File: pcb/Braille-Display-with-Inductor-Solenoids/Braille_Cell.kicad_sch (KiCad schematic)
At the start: 12 parts, among them U2 AD116, U3 AD116

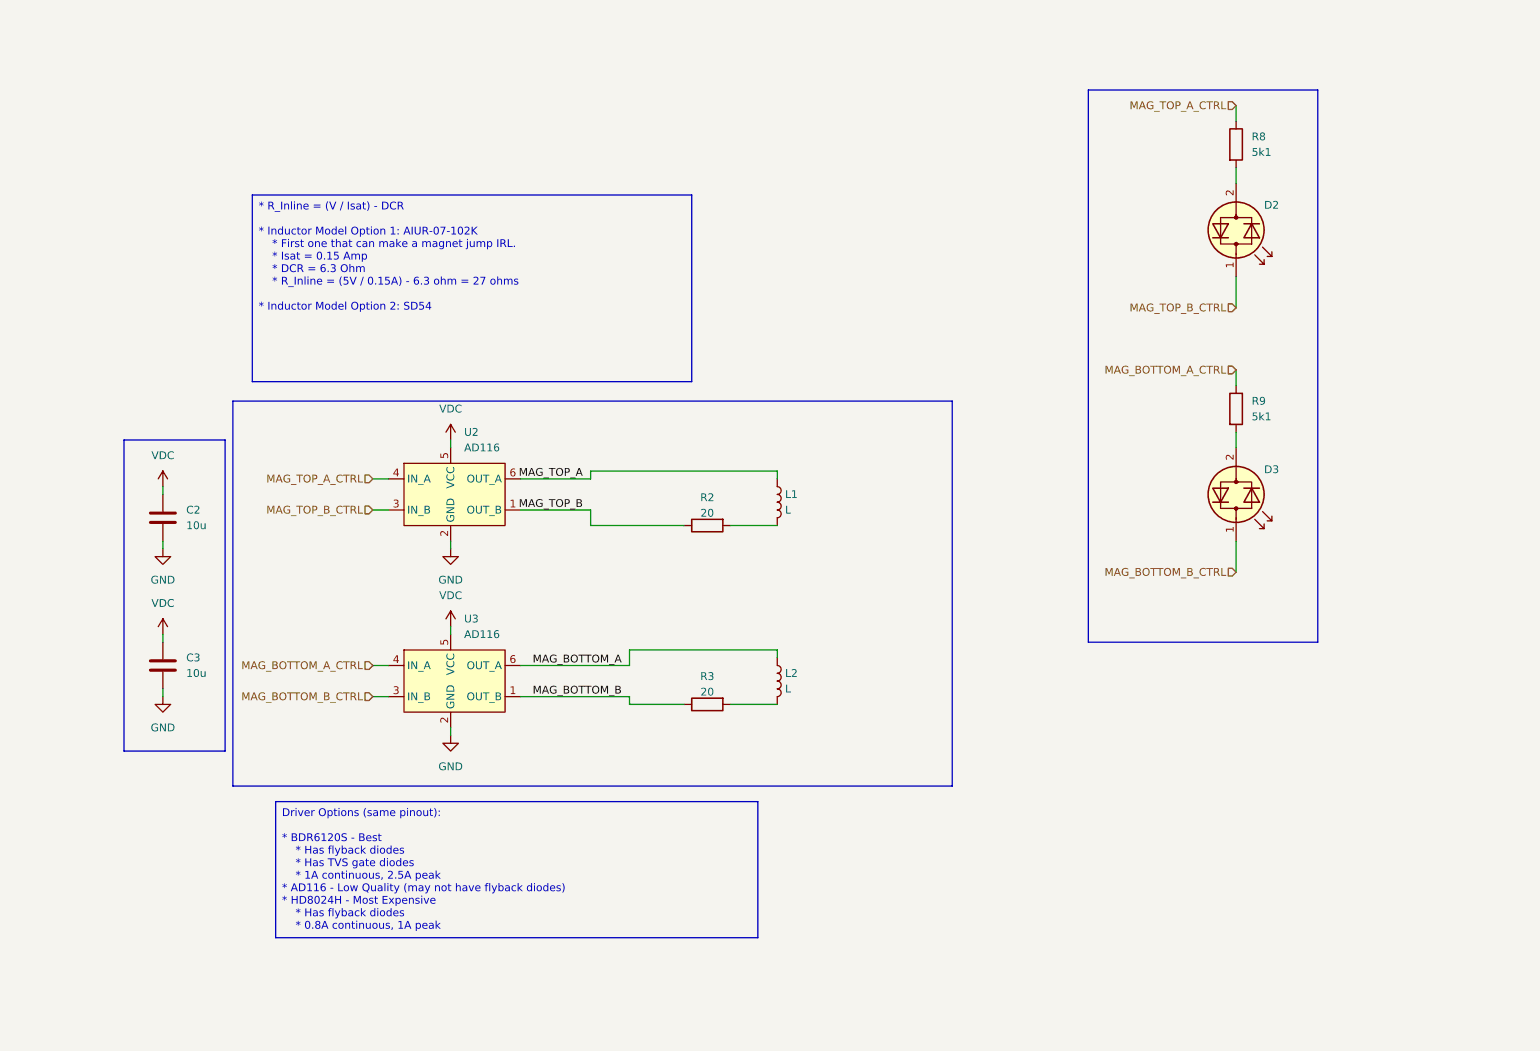
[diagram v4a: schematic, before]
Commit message: Bit of tiny routing, export production file
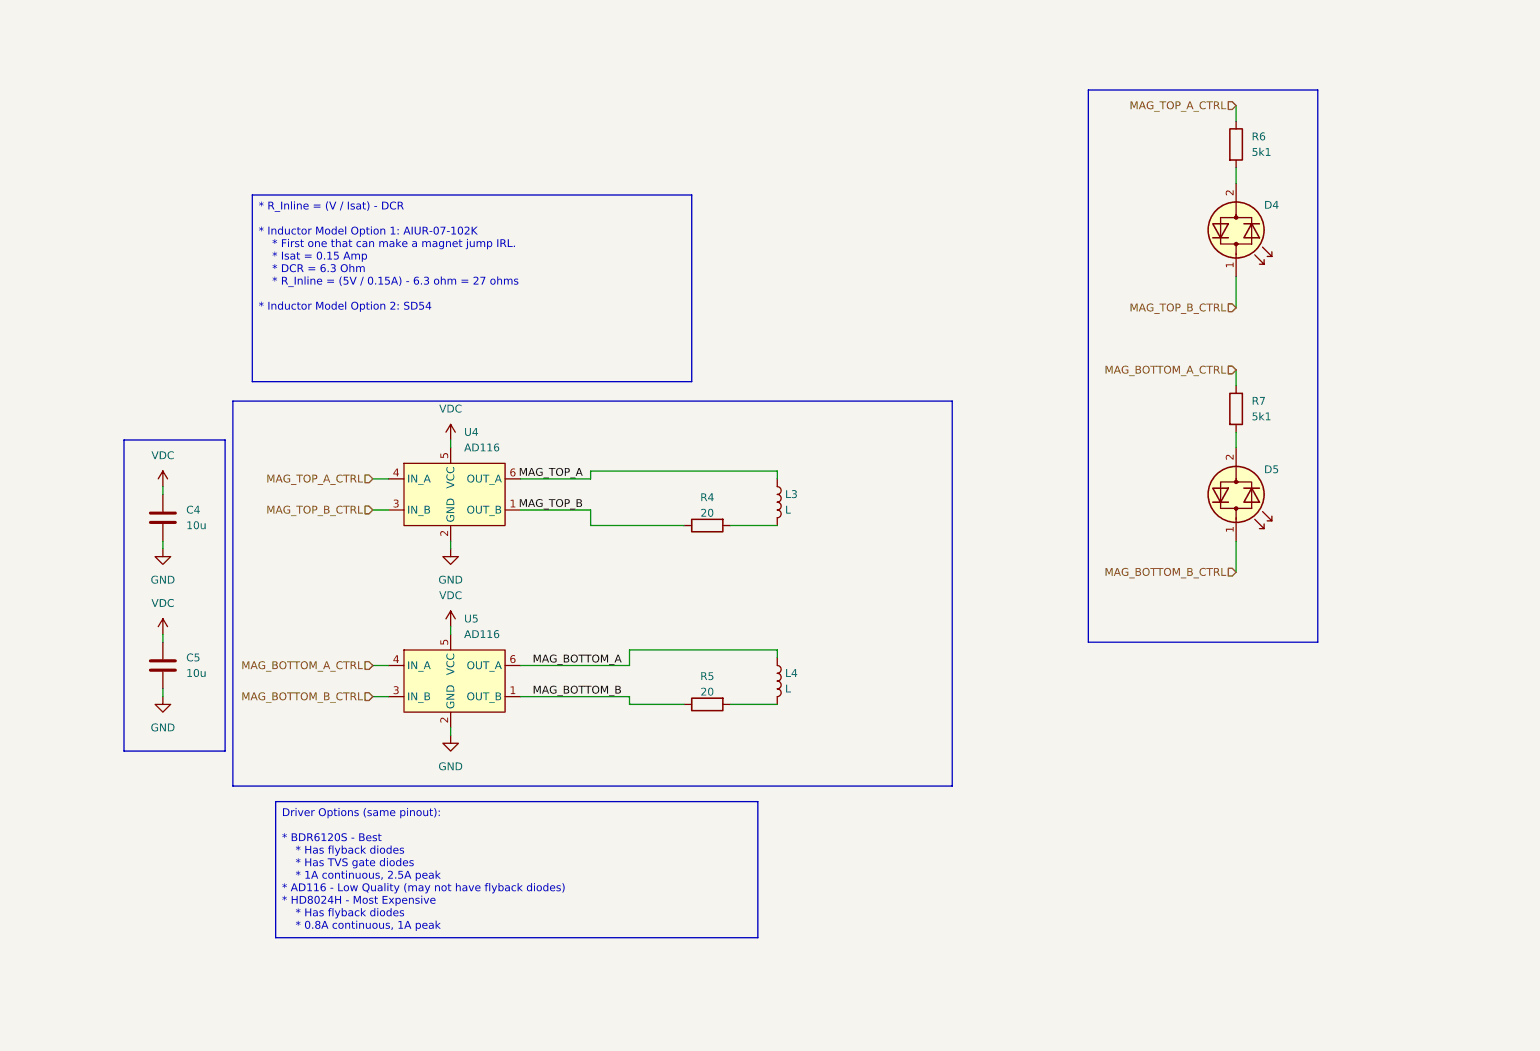
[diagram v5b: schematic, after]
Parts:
- renumbered C2 to C4, C3 to C5, D2 to D4, D3 to D5, L1 to L3, L2 to L4, R2 to R4, R3 to R5, R8 to R6, R9 to R7, U2 to U4, U3 to U5
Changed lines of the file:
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@@
 		(dnp no)
 		(fields_autoplaced yes)
-		(property "Reference" "#PWR031"
+		(property "Reference" "#PWR027"
 			(at 87.63 118.11 0)
 			(effects
@@
 		(on_board yes)
 		(dnp no)
-		(property "Reference" "D3"
+		(property "Reference" "D5"
 			(at 220.472 88.646 90)
 			(effects
@@
 		(dnp no)
 		(fields_autoplaced yes)
-		(property "Reference" "L2"
+		(property "Reference" "L4"
 			(at 142.24 121.9199 0)
 			(effects
@@
 		(on_board yes)
 		(dnp no)
-		(property "Reference" "D2"
+		(property "Reference" "D4"
 			(at 220.472 45.466 90)
 			(effects
@@
 		(dnp no)
 		(fields_autoplaced yes)
-		(property "Reference" "#PWR018"
+		(property "Reference" "#PWR022"
 			(at 40.64 107.95 0)
 			(effects
@@
 		(dnp no)
 		(fields_autoplaced yes)
-		(property "Reference" "#PWR020"
+		(property "Reference" "#PWR024"
 			(at 40.64 132.08 0)
 			(effects
@@
 		(dnp no)
 		(fields_autoplaced yes)
-		(property "Reference" "R9"
+		(property "Reference" "R7"
 			(at 218.44 77.4699 0)
 			(effects
@@
 		(on_board yes)
 		(dnp no)
-		(property "Reference" "R2"
+		(property "Reference" "R4"
 			(at 129.54 93.218 90)
 			(effects
@@
 		(dnp no)
 		(fields_autoplaced yes)
-		(property "Reference" "C2"
+		(property "Reference" "C4"
 			(at 44.45 95.2499 0)
 			(effects
@@
 		(dnp no)
 		(fields_autoplaced yes)
-		(property "Reference" "#PWR019"
+		(property "Reference" "#PWR023"
 			(at 40.64 119.38 0)
 			(effects
@@
 		(dnp no)
 		(fields_autoplaced yes)
-		(property "Reference" "L1"
+		(property "Reference" "L3"
 			(at 142.24 92.7099 0)
 			(effects
@@
 		(dnp no)
 		(fields_autoplaced yes)
-		(property "Reference" "C3"
+		(property "Reference" "C5"
 			(at 44.45 119.3799 0)
 			(effects
@@
 		(dnp no)
 		(fields_autoplaced yes)
-		(property "Reference" "U2"
+		(property "Reference" "U4"
 			(at 89.8241 82.55 0)
 			(effects
@@
 		(on_board yes)
 		(dnp no)
-		(property "Reference" "R3"
+		(property "Reference" "R5"
 			(at 129.54 122.428 90)
 			(effects
@@
 		(dnp no)
 		(fields_autoplaced yes)
-		(property "Reference" "R8"
+		(property "Reference" "R6"
 			(at 218.44 34.2899 0)
 			(effects
@@
 		(dnp no)
 		(fields_autoplaced yes)
-		(property "Reference" "#PWR017"
+		(property "Reference" "#PWR021"
 			(at 40.64 95.25 0)
 			(effects
@@
 		(dnp no)
 		(fields_autoplaced yes)
-		(property "Reference" "#PWR029"
+		(property "Reference" "#PWR025"
 			(at 87.63 87.63 0)
 			(effects
@@
 		(dnp no)
 		(fields_autoplaced yes)
-		(property "Reference" "#PWR032"
+		(property "Reference" "#PWR028"
 			(at 87.63 138.43 0)
 			(effects
@@
 		(dnp no)
 		(fields_autoplaced yes)
-		(property "Reference" "U3"
+		(property "Reference" "U5"
 			(at 89.8241 113.03 0)
 			(effects
@@
 		(dnp no)
 		(fields_autoplaced yes)
-		(property "Reference" "#PWR030"
+		(property "Reference" "#PWR026"
 			(at 87.63 107.95 0)
 			(effects

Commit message: pcb: Migrate to KiCAD v9
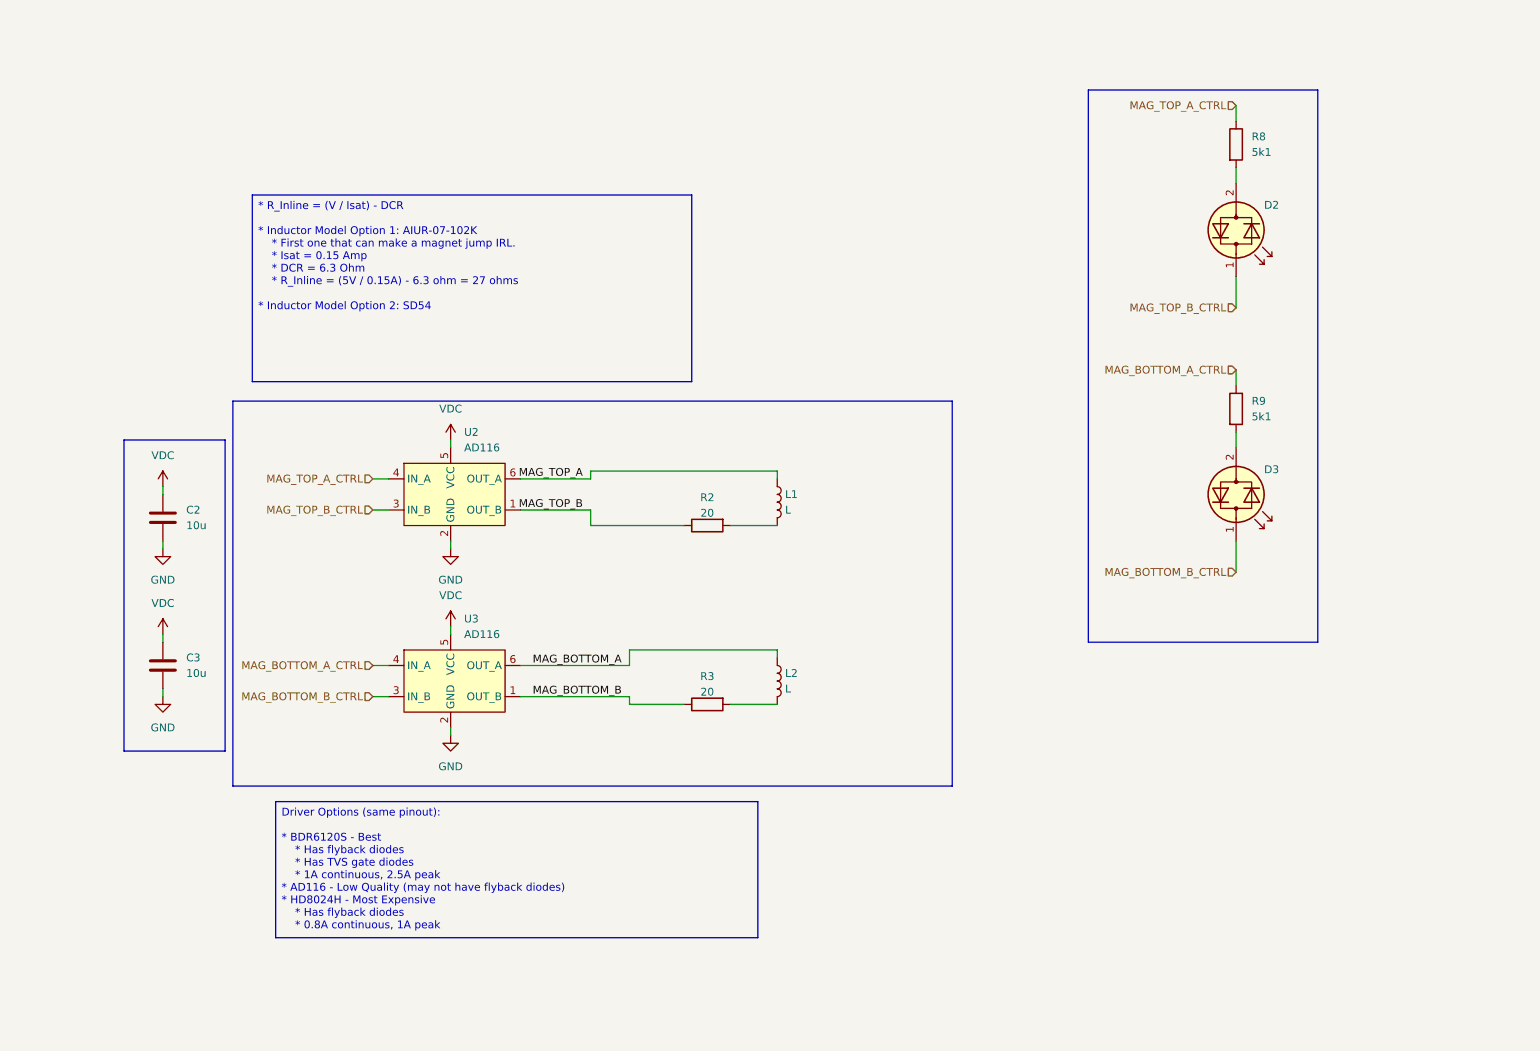
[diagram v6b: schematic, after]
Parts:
- renumbered C4 to C2, C5 to C3, D4 to D2, D5 to D3, L3 to L1, L4 to L2, R4 to R2, R5 to R3, R6 to R8, R7 to R9, U4 to U2, U5 to U3

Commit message: pcb: WIP - Switch to new parts, layout
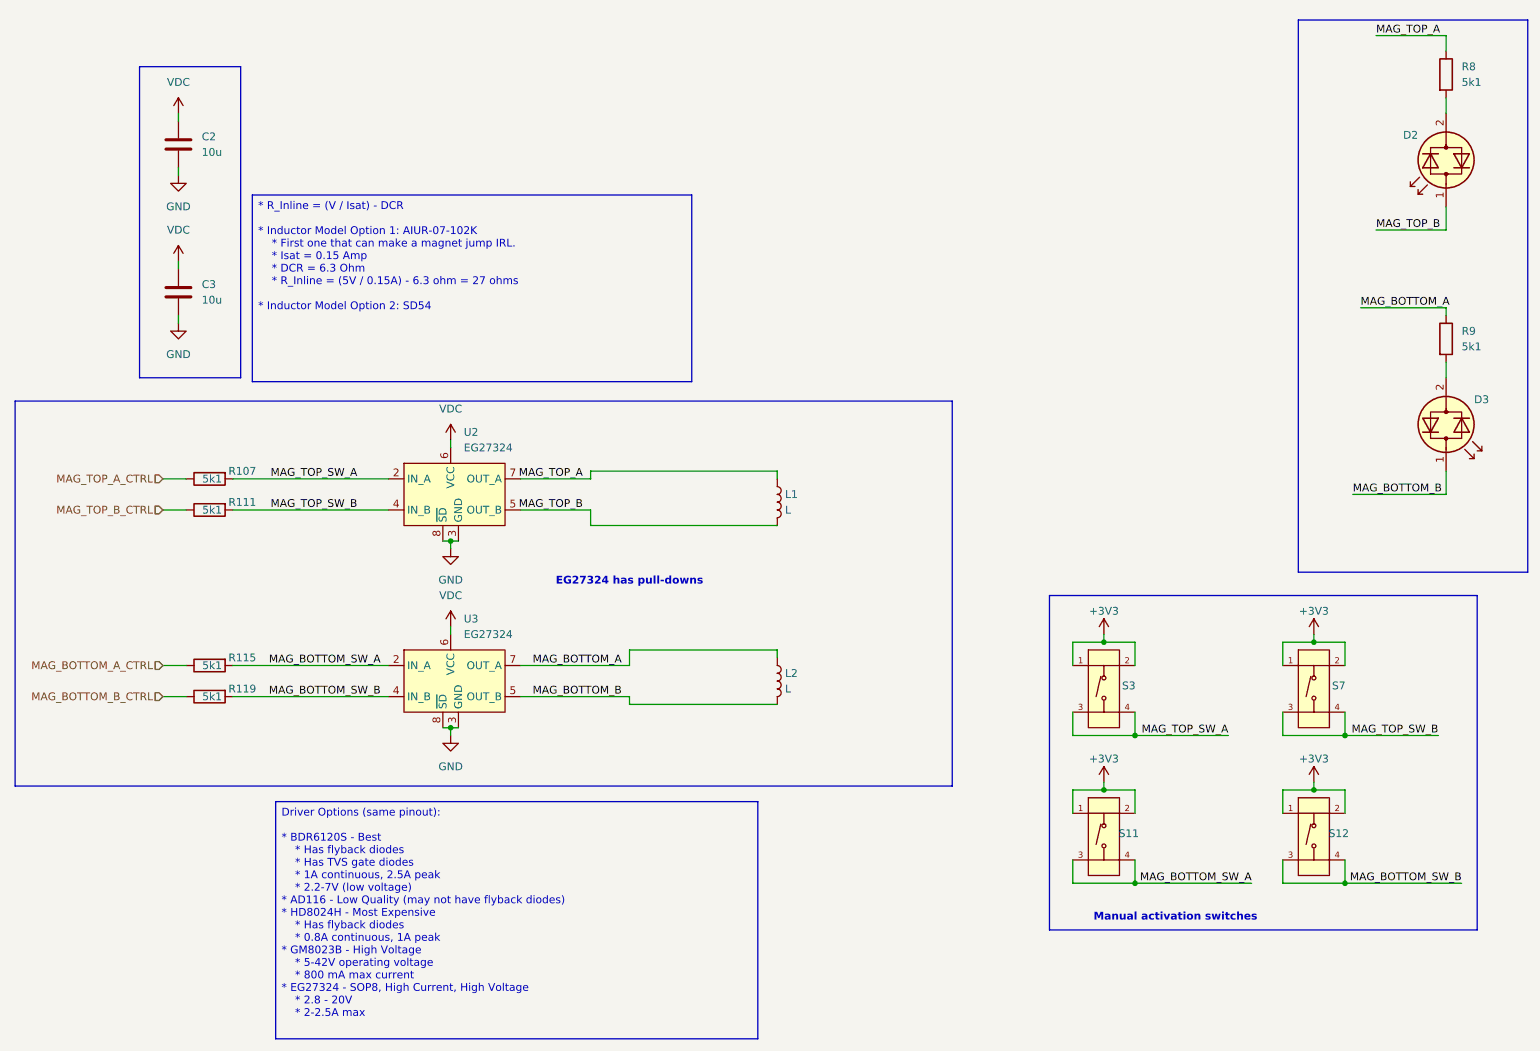
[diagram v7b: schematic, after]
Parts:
- removed R2, R3: 20, Resistor_SMD:R_2512_6332Metric_Pad1.40x3.35mm_HandSolder, symbol Device:R
- added R107, R111, R115, R119: 5k1, Resistor_SMD:R_0603_1608Metric_Pad0.98x0.95mm_HandSolder, symbol Device:R
- added S11, S12, S3, S7: Tactile Button, 160gf, PCM_JLCPCB:SW-SMD_4P-L5.1-W5.1-P3.70-LS6.5-TL-2, symbol PCM_JLCPCB-Connectors_Buttons:Tactile Button, 160gf
- U2, U3: value AD116 -> EG27324; footprint Package_TO_SOT_SMD:SOT-23-6 -> Package_SO:SOP-8_3.9x4.9mm_P1.27mm; symbol 00-project-symbols:AD116_H_Bridge -> 00-project-symbols:EG27324_H_Bridge
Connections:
- net GND: now also U2.3 (GND), U2.8 (~{SD}), U3.3 (GND), U3.8 (~{SD}); no longer U2.2 (GND), U3.2 (GND)
- net MAG_BOTTOM_A: now also R9.1, U3.7 (OUT_A); no longer U3.6 (OUT_A)
- net MAG_BOTTOM_A_CTRL: now also R115.1; no longer R9.1, U3.4 (IN_A)
- net MAG_BOTTOM_B: now also D3.1 (KA), L2.2, U3.5 (OUT_B); no longer U3.1 (OUT_B)
- net MAG_BOTTOM_B_CTRL: now also R119.1; no longer D3.1 (KA), U3.3 (IN_B)
- net MAG_TOP_A: now also R8.1, U2.7 (OUT_A); no longer U2.6 (OUT_A)
- net MAG_TOP_A_CTRL: now also R107.1; no longer R8.1, U2.4 (IN_A)
- net MAG_TOP_B: now also D2.1 (KA), L1.2, U2.5 (OUT_B); no longer U2.1 (OUT_B)
- net MAG_TOP_B_CTRL: now also R111.1; no longer D2.1 (KA), U2.3 (IN_B)
- net VDC: now also U2.6 (VCC), U3.6 (VCC); no longer U2.5 (VCC), U3.5 (VCC)
- new net +3V3: S11.1 (A), S11.2 (B), S12.1 (A), S12.2 (B), S3.1 (A), S3.2 (B), S7.1 (A), S7.2 (B)
- new net MAG_BOTTOM_SW_A: R115.2, S11.3 (C), S11.4 (D), U3.2 (IN_A)
- new net MAG_BOTTOM_SW_B: R119.2, S12.3 (C), S12.4 (D), U3.4 (IN_B)
- new net MAG_TOP_SW_A: R107.2, S3.3 (C), S3.4 (D), U2.2 (IN_A)
- new net MAG_TOP_SW_B: R111.2, S7.3 (C), S7.4 (D), U2.4 (IN_B)
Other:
- note added: "EG27324 has pull-downs"
- note added: "Manual activation switches"
- moved on the sheet: C2, C3, D2, D3, R8, R9

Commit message: pcb: WIP - High power and repeated routing
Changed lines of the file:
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@@
 		(lib_id "PCM_JLCPCB-Connectors_Buttons:Tactile Button, 160gf")
 		(at 228.6 147.32 0)
+		(mirror y)
 		(unit 1)
 		(exclude_from_sim no)
@@
 		(dnp no)
 		(property "Reference" "S12"
-			(at 232.664 148.082 0)
+			(at 224.536 148.082 0)
 			(effects
 				(font
@@
 		)
 		(property "Datasheet" "https://www.lcsc.com/datasheet/lcsc_datasheet_2304140030_XKB-Connection-TS-1187A-B-A-B_C318884.pdf"
-			(at 226.314 147.193 0)
+			(at 230.886 147.193 0)
 			(effects
 				(font
